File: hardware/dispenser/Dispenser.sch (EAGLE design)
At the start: 70 parts, among them J1 AVR_Prog, J2 RJ45-8PTH, Q1 NFET-SO8, Q2 NFET, Q3 NFET, Q4 NFET, Q5 MOSFET-NCHANNELSMD, U1 ATMEGA168, U10 HALL-EFFECT, U2 OPAMP-DUAL, U3 OPTO-TLP185, U4 MPX5010DP, U5 VREG-5V-LDO-AP1117SOT89-3L, U6 WS2801, U7 HALL-EFFECT, U8 HALL-EFFECT, U9 HALL-EFFECT

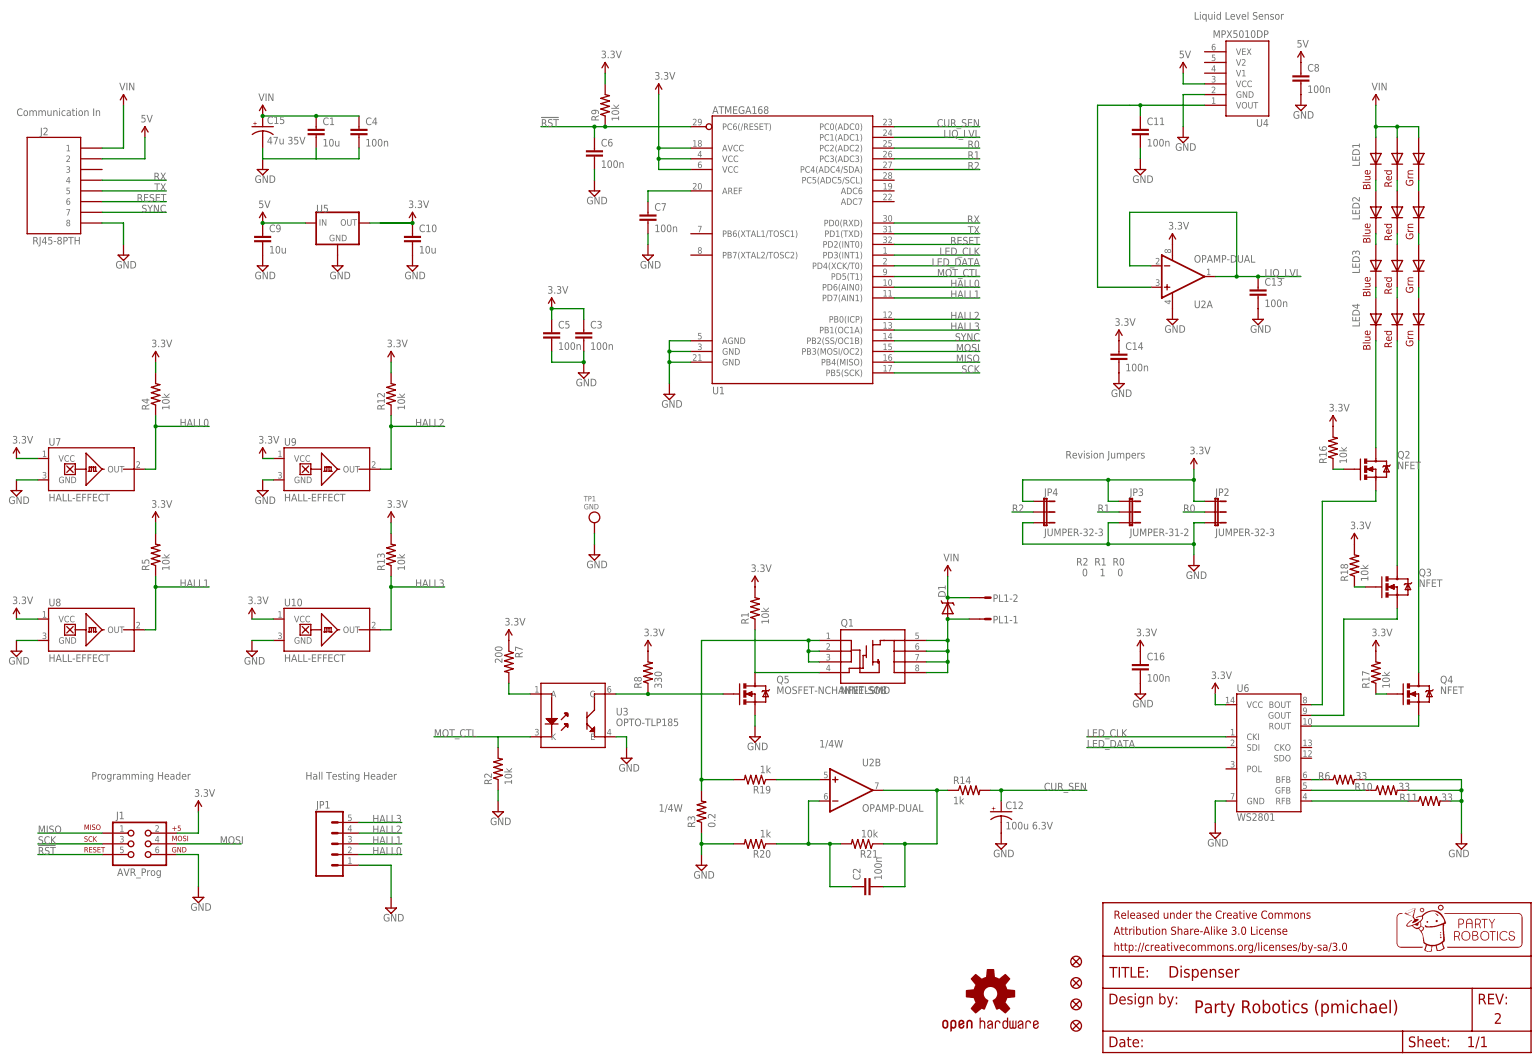
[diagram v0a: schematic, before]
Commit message: Remove annoying bottle size drop downs and fix changing dispense button
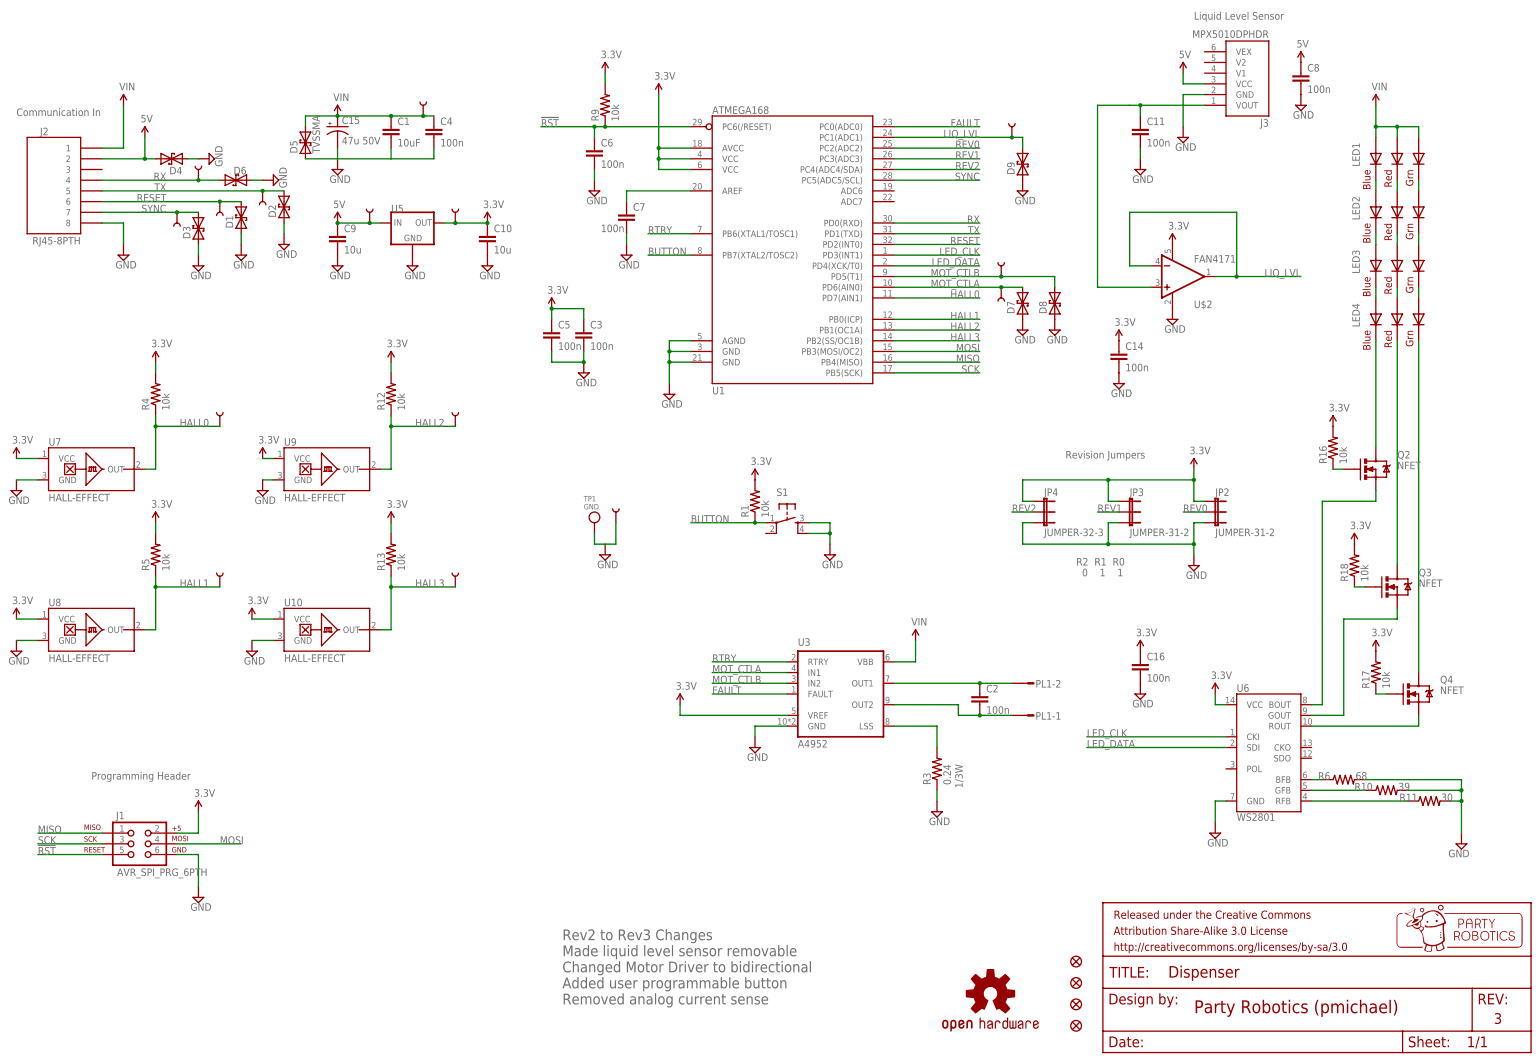
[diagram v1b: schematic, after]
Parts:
- removed C12: 100u 6.3V, SparkFun-Capacitors:CAP_POLD
- removed C13: 100n, SparkFun:CAP0603-CAP
- removed JP1: (no value), SparkFun:M051.27MM
- removed Q1: NFET-SO8, pierre:NFET-SO8
- removed Q5: MOSFET-NCHANNELSMD, SparkFun-DiscreteSemi:MOSFET-NCHANNELSMD
- removed R14, R19, R20: 1k, SparkFun-Resistors:RESISTOR0603-RES
- removed R2, R21: 10k, SparkFun-Resistors:RESISTOR0603-RES
- removed R7: 200, SparkFun-Resistors:RESISTOR0603-RES
- removed R8: 330, SparkFun-Resistors:RESISTOR0603-RES
- removed U2: OPAMP-DUAL, SparkFun-AnalogIC:OPAMP-DUALU
- removed U4: MPX5010DP, pierre:MPX5010DP
- added D2, D3, D4, D6, D7, D8, D9: TVSSOD-923, pierre:TVSSOD-923
- added D5: TVSSMA, pierre:TVSSMA
- added J3: MPX5010DPHDR, pierre:MPX5010DPHDR
- added S1: (no value), pierre:TAC_SWITCHSMD
- added TP10, TP11, TP12, TP7, TP8, TP9: TEST-POINT3X5, SparkFun-Passives:TEST-POINT3X5
- added TP13, TP14, TP15, TP16, TP2, TP3, TP4, TP5, TP6: TEST-POINT0.08, pierre:TEST-POINT0.08
- added U$2: FAN4171, SparkFun-AnalogIC:OPA344
- C1: value 10u -> 10uF; device SparkFun-Passives:CAP0603-CAP -> SparkFun-Capacitors:2.2UF-CERCAP-10009
- C15: value 47u 35V -> 47u 50V
- D1: value (none) -> TVSSOD-923; device pierre:B330A -> pierre:TVSSOD-923
- J1: value AVR_Prog -> AVR_SPI_PRG_6PTH; device SparkFun-Connectors:AVR_SPI_PRG_62X3_LOCK -> SparkFun-Connectors:AVR_SPI_PRG_6PTH
- JP2: value JUMPER-32-3 -> JUMPER-31-2; device SparkFun-Passives:JUMPER-32-3 -> SparkFun-Passives:JUMPER-31-2
- R10: value 33 -> 39
- R11: value 33 -> 30
- R3: value 0.2 -> 0.24
- R6: value 33 -> 68
- U3: value OPTO-TLP185 -> A4952; device pierre:OPTO-TLP185 -> pierre:A4952
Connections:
- net R0 renamed REV0
- net R1 renamed REV1
- net R2 renamed REV2
- removed net 1/4W: Q1.S@1, Q1.S@2, Q1.S@3, R19.2, R3.2
- removed net CUR_SEN: C12.+, R14.2, U1.PC0(ADC0)
- removed net MOT_B: D1.A, PL1-1.S, Q1.D@1, Q1.D@2, Q1.D@3, Q1.D@4
- removed net MOT_CTL: R2.2, U1.PD5(T1), U3.K
- removed net MOT_CUR: C2.2, R14.1, R21.1, U2B.OUT
- removed net N$11: R19.1, U2B.+IN
- removed net N$16: R7.2, U3.A
- removed net N$31: Q5.G, R8.1, U3.C
- new net 1/3W: R3.2, U3.LSS
- new net BUTTON: R1.1, S1.1, U1.PB7(XTAL2/TOSC2)
- new net FAULT: U1.PC0(ADC0), U3.FAULT
- new net MOT_CTLA: D7.2, TP8.1, U1.PD6(AIN0), U3.IN1
- new net MOT_CTLB: D8.2, TP7.1, U1.PD5(T1), U3.IN2
- new net RTRY: U1.PB6(XTAL1/TOSC1), U3.RTRY
- net 3.3V: now also TP16.1, U$2.V+, U3.VREF; no longer C8.1, R7.1, R8.2, U2A.V+
- net 5V: now also C8.1, D4.2, J3.VCC, TP3.1; no longer U4.VCC
- net GND: now also D1.1, D2.1, D3.1, D4.1, D5.1, D6.1, D7.1, D8.1, D9.1, J3.GND, S1.3, S1.4, TP2.1, U$2.V-, U3.GND; no longer C12.-, C13.2, JP1.1, Q5.S, R2.1, R20.2, U2A.V-, U3.E, U4.GND
- net HALL0: now also TP10.1, U1.PD7(AIN1); no longer JP1.2, U1.PD6(AIN0)
- net HALL1: now also TP11.1, U1.PB0(ICP); no longer JP1.3, U1.PD7(AIN1)
- net HALL2: now also TP9.1, U1.PB1(OC1A); no longer JP1.4, U1.PB0(ICP)
- net HALL3: now also TP12.1, U1.PB2(SS/OC1B); no longer JP1.5, U1.PB1(OC1A)
- net LIQ_LVL: now also D9.2, TP14.1, U$2.-IN, U$2.OUT; no longer C13.1, U2A.-IN, U2A.OUT
- net N$10: now also C2.2, PL1-1.S, U3.OUT2; no longer C2.1, R20.1, R21.2, U2B.-IN
- net N$26: now also J3.VOUT, U$2.+IN; no longer U2A.+IN, U4.VOUT
- net N$9: now also C2.1, PL1-2.S, U3.OUT1; no longer Q1.G, Q5.D, R1.1
- net RESET: now also D1.2, TP13.1
- net RX: now also D6.2, TP4.1
- net SYNC: now also D3.2, TP15.1, U1.PC5(ADC5/SCL); no longer U1.PB2(SS/OC1B)
- net TX: now also D2.2, TP5.1
- net VIN: now also D5.2, TP6.1, U3.VBB; no longer D1.C, PL1-2.S
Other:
- note added: "0 1 1"
- note added: "3"
- note added: "Rev2 to Rev3 Changes Made liquid level sensor removable Changed Motor Driver to bidirectional Added user programmable button Removed analog current sense"
- note removed: "0 1 0"
- note removed: "2"
- note removed: "Hall Testing Header"
- moved on the sheet: C1, C10, C15, C2, C4, C7, C9, PL1-1, PL1-2, R1, R3, U5
